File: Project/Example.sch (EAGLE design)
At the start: 13 parts, among them IC1 LM555D, J2 UX60-MB-5S8, Q1 BSS806N, Q2 SSM3J356R, SW1 MFS101D-6-Z

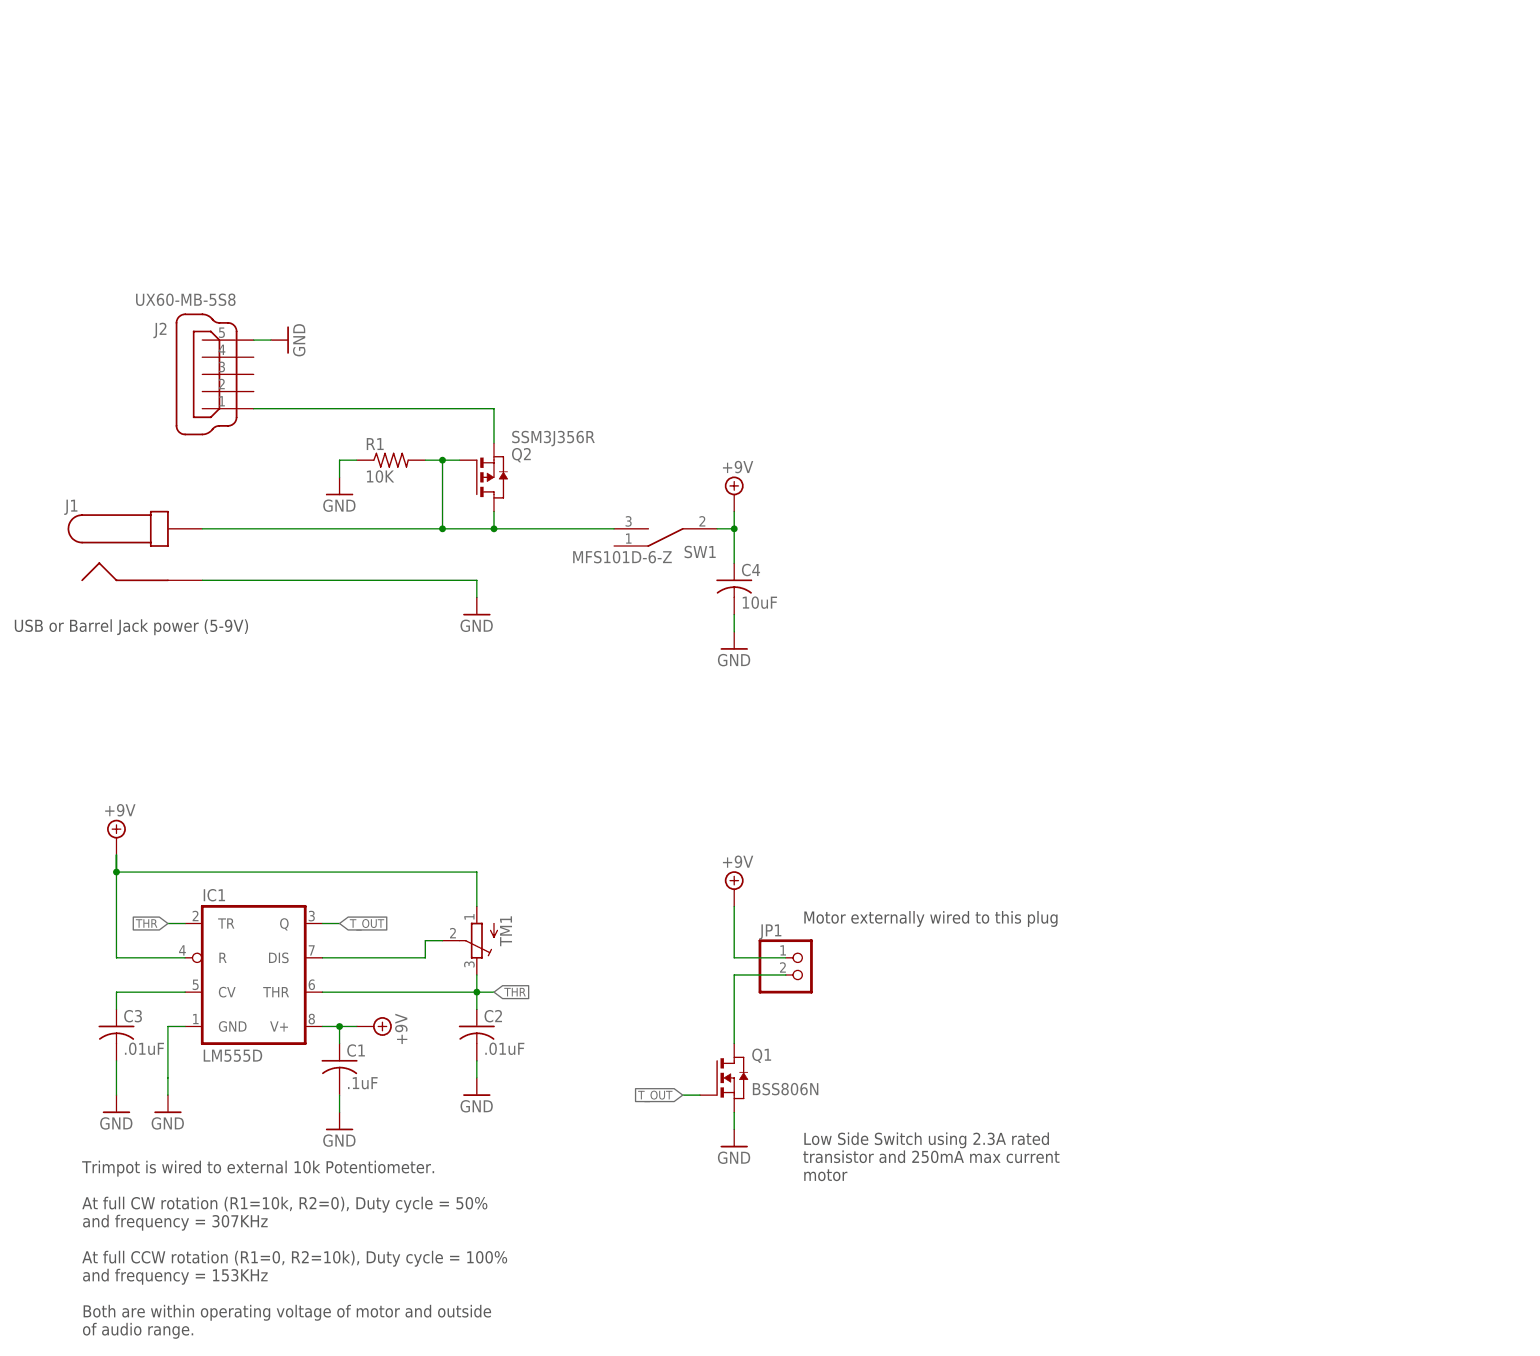
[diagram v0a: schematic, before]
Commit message: Made schematic neater
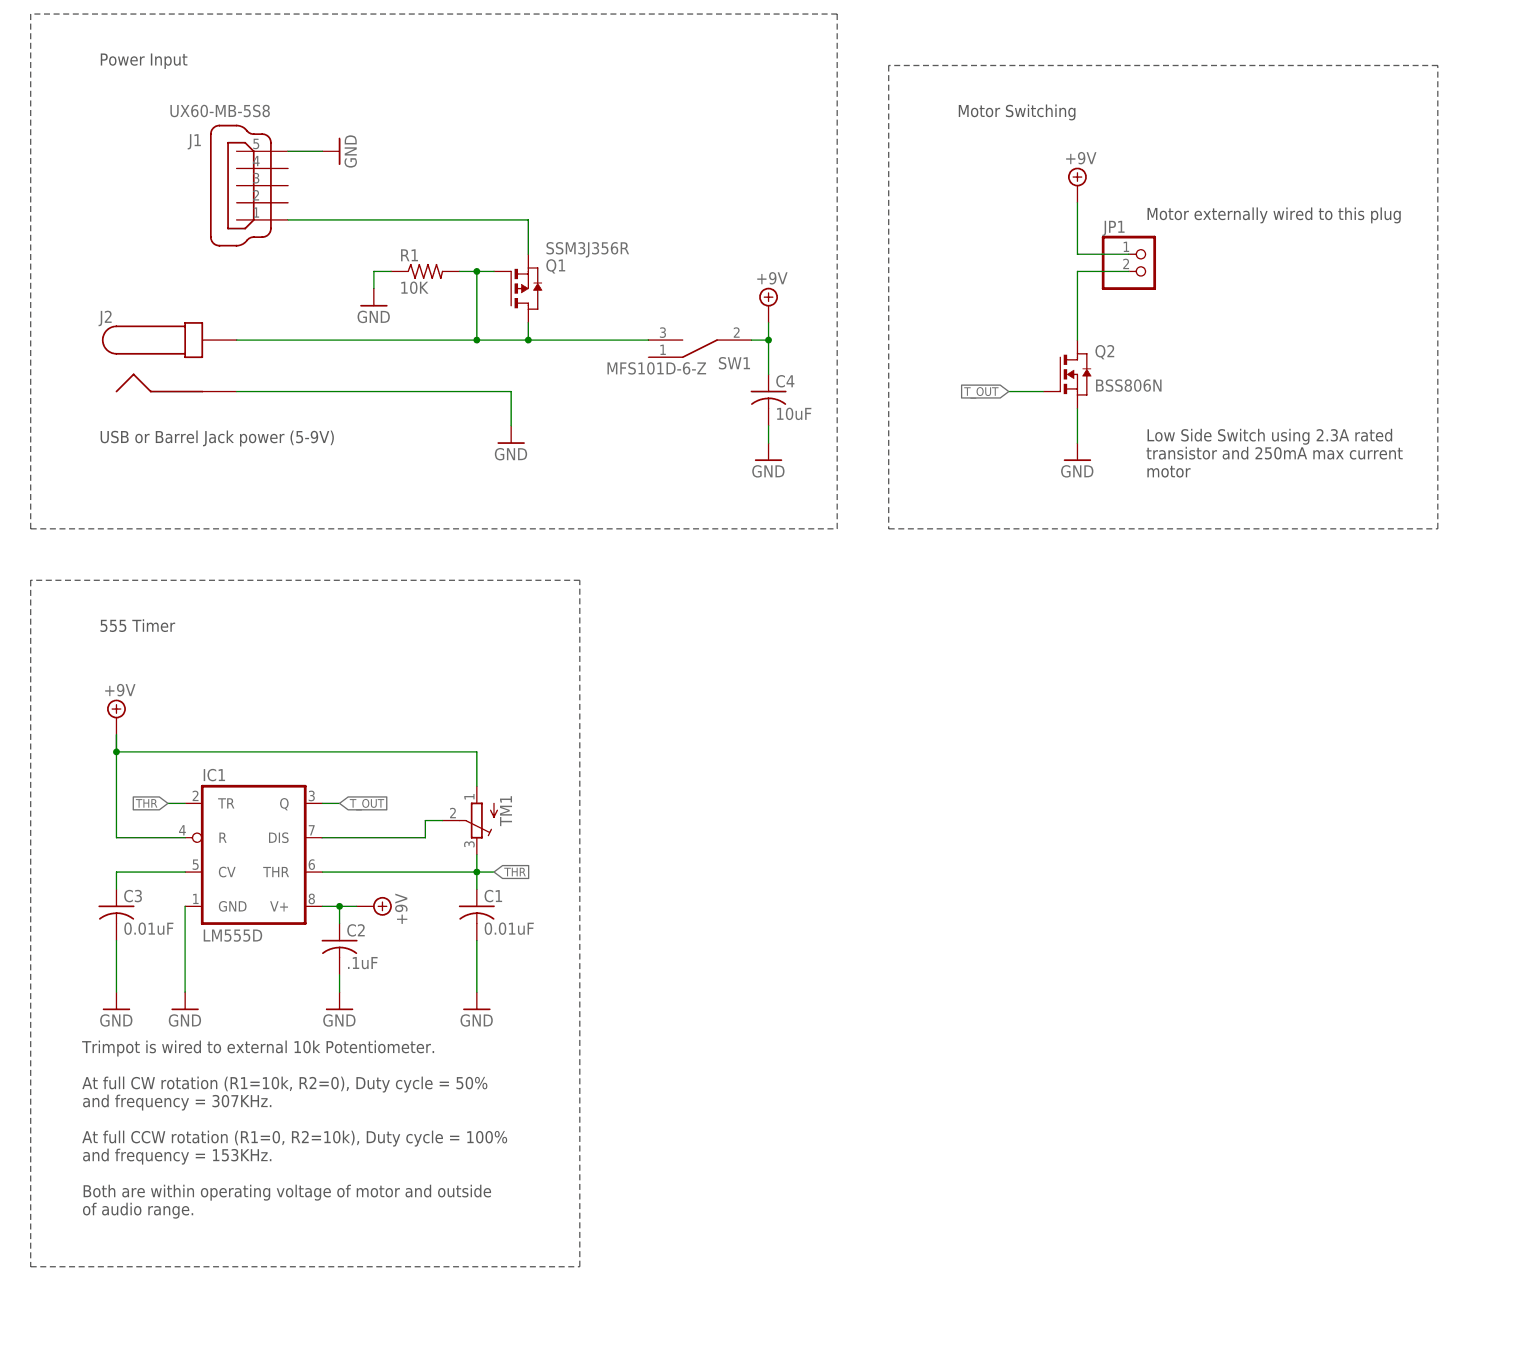
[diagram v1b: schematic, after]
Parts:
- C1: value .1uF -> 0.01uF
- C2: value .01uF -> .1uF
- C3: value .01uF -> 0.01uF
- J1: value (none) -> UX60-MB-5S8; device RoboJackets-Connectors:PJ-037A -> RoboJackets-Connectors:UX60-MB-5S8
- J2: value UX60-MB-5S8 -> (none); device RoboJackets-Connectors:UX60-MB-5S8 -> RoboJackets-Connectors:PJ-037A
- Q1: value BSS806N -> SSM3J356R; device RoboJackets-Discrete:BSS806N -> Example:SSM3J356R
- Q2: value SSM3J356R -> BSS806N; device Example:SSM3J356R -> RoboJackets-Discrete:BSS806N
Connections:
- net +9V: now also C2.1; no longer C1.1
- net GND: now also J1.5, J2.2, Q2.S; no longer J1.2, J2.5, Q1.S
- net N$2: now also Q2.D; no longer Q1.D
- net N$4: now also J1.1, Q1.S; no longer J2.1, Q2.S
- net N$6: now also J2.1, Q1.D, Q1.G; no longer J1.1, Q2.D, Q2.G
- net THR: now also C1.1; no longer C2.1
- net T_OUT: now also Q2.G; no longer Q1.G
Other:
- note added: "555 Timer"
- note added: "Motor Switching"
- note added: "Power Input"
- note added: "Trimpot is wired to external 10k Potentiometer. At full CW rotation (R1=10k, R2=0), Duty cycle = 50% and frequency = 307KHz. At full CCW rotation (R1=0, R2=10k), Duty cycle = 100% and frequency = 153KHz. Both are within operating voltage of motor and outside of audio range."
- note removed: "Trimpot is wired to external 10k Potentiometer. At full CW rotation (R1=10k, R2=0), Duty cycle = 50% and frequency = 307KHz At full CCW rotation (R1=0, R2=10k), Duty cycle = 100% and frequency = 153KHz Both are within operating voltage of motor and outside of audio range."
- moved on the sheet: C1, C2, C3, C4, IC1, JP1, Q1, Q2, R1, SW1, TM1

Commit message: Cleaning up example
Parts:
- C2: value .1uF -> 0.1uF
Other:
- note added: "Low side switch using 2.3A rated transistor and 450mA max current motor"
- note added: "Trimpot is wired to external 10K Potentiometer. At full CW rotation (R1=10K, R2=0), Duty cycle = 50% and frequency = 307KHz. At full CCW rotation (R1=0, R2=10K), Duty cycle = 100% and frequency = 153KHz. Both are within operating voltage of motor and outside of audio range."
- note removed: "Low Side Switch using 2.3A rated transistor and 250mA max current motor"
- note removed: "Trimpot is wired to external 10k Potentiometer. At full CW rotation (R1=10k, R2=0), Duty cycle = 50% and frequency = 307KHz. At full CCW rotation (R1=0, R2=10k), Duty cycle = 100% and frequency = 153KHz. Both are within operating voltage of motor and outside of audio range."
- moved on the sheet: JP1, Q2
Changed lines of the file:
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@@
 <part name="SUPPLY1" library="RoboJackets-Supplies" deviceset="+9V" device=""/>
 <part name="SUPPLY2" library="RoboJackets-Supplies" deviceset="+9V" device=""/>
-<part name="C2" library="rcl" library_urn="urn:adsk.eagle:library:334" deviceset="C-US" device="C0603" package3d_urn="urn:adsk.eagle:package:23616/2" value=".1uF"/>
+<part name="C2" library="rcl" library_urn="urn:adsk.eagle:library:334" deviceset="C-US" device="C0603" package3d_urn="urn:adsk.eagle:package:23616/2" value="0.1uF"/>
 <part name="C1" library="rcl" library_urn="urn:adsk.eagle:library:334" deviceset="C-US" device="C0603" package3d_urn="urn:adsk.eagle:package:23616/2" value="0.01uF"/>
 <part name="SUPPLY3" library="RoboJackets-Supplies" deviceset="GND" device=""/>
@@
 <description>555 Timer Motor Driver Circuit</description>
 <plain>
-<text x="22.86" y="25.4" size="1.778" layer="97">Trimpot is wired to external 10k Potentiometer.
-At full CW rotation (R1=10k, R2=0), Duty cycle = 50%
+<text x="25.4" y="25.4" size="1.778" layer="97">Trimpot is wired to external 10K Potentiometer.
+At full CW rotation (R1=10K, R2=0), Duty cycle = 50%
 and frequency = 307KHz.
-At full CCW rotation (R1=0, R2=10k), Duty cycle = 100%
+At full CCW rotation (R1=0, R2=10K), Duty cycle = 100%
 and frequency = 153KHz.
 Both are within operating voltage of motor and outside
 of audio range. </text>
-<text x="180.34" y="172.72" size="1.778" layer="97">Motor externally wired to this plug</text>
-<text x="180.34" y="134.62" size="1.778" layer="97">Low Side Switch using 2.3A rated
-transistor and 250mA max current
+<text x="182.88" y="172.72" size="1.778" layer="97">Motor externally wired to this plug</text>
+<text x="182.88" y="134.62" size="1.778" layer="97">Low side switch using 2.3A rated
+transistor and 450mA max current
 motor</text>
 <text x="25.4" y="139.7" size="1.778" layer="97">USB or Barrel Jack power (5-9V)</text>
-<wire x1="15.24" y1="127" x2="134.62" y2="127" width="0.1524" layer="97" style="shortdash"/>
-<wire x1="134.62" y1="127" x2="134.62" y2="203.2" width="0.1524" layer="97" style="shortdash"/>
-<wire x1="134.62" y1="203.2" x2="15.24" y2="203.2" width="0.1524" layer="97" style="shortdash"/>
+<wire x1="15.24" y1="127" x2="137.16" y2="127" width="0.1524" layer="97" style="shortdash"/>
+<wire x1="137.16" y1="127" x2="137.16" y2="203.2" width="0.1524" layer="97" style="shortdash"/>
+<wire x1="137.16" y1="203.2" x2="15.24" y2="203.2" width="0.1524" layer="97" style="shortdash"/>
 <wire x1="15.24" y1="203.2" x2="15.24" y2="127" width="0.1524" layer="97" style="shortdash"/>
 <text x="25.4" y="195.58" size="1.778" layer="97">Power Input</text>
 <wire x1="15.24" y1="119.38" x2="15.24" y2="17.78" width="0.1524" layer="97" style="shortdash"/>
-<wire x1="15.24" y1="17.78" x2="96.52" y2="17.78" width="0.1524" layer="97" style="shortdash"/>
-<wire x1="96.52" y1="17.78" x2="96.52" y2="119.38" width="0.1524" layer="97" style="shortdash"/>
-<wire x1="96.52" y1="119.38" x2="15.24" y2="119.38" width="0.1524" layer="97" style="shortdash"/>
+<wire x1="15.24" y1="17.78" x2="99.06" y2="17.78" width="0.1524" layer="97" style="shortdash"/>
+<wire x1="99.06" y1="17.78" x2="99.06" y2="119.38" width="0.1524" layer="97" style="shortdash"/>
+<wire x1="99.06" y1="119.38" x2="15.24" y2="119.38" width="0.1524" layer="97" style="shortdash"/>
 <text x="25.4" y="111.76" size="1.778" layer="97">555 Timer</text>
-<wire x1="142.24" y1="127" x2="223.52" y2="127" width="0.1524" layer="97" style="shortdash"/>
-<wire x1="223.52" y1="127" x2="223.52" y2="195.58" width="0.1524" layer="97" style="shortdash"/>
-<wire x1="223.52" y1="195.58" x2="142.24" y2="195.58" width="0.1524" layer="97" style="shortdash"/>
-<wire x1="142.24" y1="195.58" x2="142.24" y2="127" width="0.1524" layer="97" style="shortdash"/>
-<text x="152.4" y="187.96" size="1.778" layer="97">Motor Switching</text>
+<wire x1="144.78" y1="127" x2="228.6" y2="127" width="0.1524" layer="97" style="shortdash"/>
+<wire x1="228.6" y1="127" x2="228.6" y2="195.58" width="0.1524" layer="97" style="shortdash"/>
+<wire x1="228.6" y1="195.58" x2="144.78" y2="195.58" width="0.1524" layer="97" style="shortdash"/>
+<wire x1="144.78" y1="195.58" x2="144.78" y2="127" width="0.1524" layer="97" style="shortdash"/>
+<text x="154.94" y="187.96" size="1.778" layer="97">Motor Switching</text>
 </plain>
 <instances>
@@
 <attribute name="VALUE" x="28.956" y="66.929" size="1.778" layer="96"/>
 </instance>
-<instance part="Q2" gate="G$1" x="170.18" y="149.86" smashed="yes">
-<attribute name="VALUE" x="172.72" y="147.32" size="1.778" layer="96"/>
-<attribute name="NAME" x="172.72" y="152.4" size="1.778" layer="95"/>
-</instance>
-<instance part="SUPPLY6" gate="G$1" x="170.18" y="137.16" smashed="yes">
-<attribute name="VALUE" x="167.64" y="134.62" size="1.778" layer="96"/>
+<instance part="Q2" gate="G$1" x="172.72" y="149.86" smashed="yes">
+<attribute name="VALUE" x="175.26" y="147.32" size="1.778" layer="96"/>
+<attribute name="NAME" x="175.26" y="152.4" size="1.778" layer="95"/>
+</instance>
+<instance part="SUPPLY6" gate="G$1" x="172.72" y="137.16" smashed="yes">
+<attribute name="VALUE" x="170.18" y="134.62" size="1.778" layer="96"/>
 </instance>
 <instance part="J2" gate="G$1" x="35.56" y="149.86" smashed="yes">
@@
 <attribute name="VALUE" x="25.4" y="144.78" size="1.778" layer="96"/>
 </instance>
-<instance part="JP1" gate="G$1" x="180.34" y="165.1" smashed="yes">
-<attribute name="NAME" x="173.99" y="170.815" size="1.778" layer="95"/>
-<attribute name="VALUE" x="173.99" y="160.02" size="1.778" layer="96"/>
-</instance>
-<instance part="SUPPLY7" gate="+9V" x="170.18" y="177.8" smashed="yes">
-<attribute name="VALUE" x="168.275" y="180.975" size="1.778" layer="96"/>
-</instance>
-<instance part="SUPPLY8" gate="G$1" x="86.36" y="139.7" smashed="yes">
-<attribute name="VALUE" x="83.82" y="137.16" size="1.778" layer="96"/>
+<instance part="JP1" gate="G$1" x="182.88" y="165.1" smashed="yes">
+<attribute name="NAME" x="176.53" y="170.815" size="1.778" layer="95"/>
+<attribute name="VALUE" x="176.53" y="160.02" size="1.778" layer="96"/>
+</instance>
+<instance part="SUPPLY7" gate="+9V" x="172.72" y="177.8" smashed="yes">
+<attribute name="VALUE" x="170.815" y="180.975" size="1.778" layer="96"/>
+</instance>
+<instance part="SUPPLY8" gate="G$1" x="86.36" y="137.16" smashed="yes">
+<attribute name="VALUE" x="83.82" y="134.62" size="1.778" layer="96"/>
 </instance>
 <instance part="SUPPLY9" gate="+9V" x="124.46" y="160.02" smashed="yes">
@@
 <pinref part="SUPPLY6" gate="G$1" pin="GND"/>
 <pinref part="Q2" gate="G$1" pin="S"/>
-<wire x1="170.18" y1="139.7" x2="170.18" y2="144.78" width="0.1524" layer="91"/>
+<wire x1="172.72" y1="139.7" x2="172.72" y2="144.78" width="0.1524" layer="91"/>
 </segment>
 <segment>
@@
 <wire x1="45.72" y1="147.32" x2="86.36" y2="147.32" width="0.1524" layer="91"/>
 <pinref part="SUPPLY8" gate="G$1" pin="GND"/>
-<wire x1="86.36" y1="147.32" x2="86.36" y2="142.24" width="0.1524" layer="91"/>
+<wire x1="86.36" y1="147.32" x2="86.36" y2="139.7" width="0.1524" layer="91"/>
 </segment>
 <segment>
@@
 <segment>
 <pinref part="JP1" gate="G$1" pin="1"/>
-<wire x1="177.8" y1="167.64" x2="170.18" y2="167.64" width="0.1524" layer="91"/>
-<wire x1="170.18" y1="167.64" x2="170.18" y2="175.26" width="0.1524" layer="91"/>
+<wire x1="180.34" y1="167.64" x2="172.72" y2="167.64" width="0.1524" layer="91"/>
+<wire x1="172.72" y1="167.64" x2="172.72" y2="175.26" width="0.1524" layer="91"/>
 <pinref part="SUPPLY7" gate="+9V" pin="+9V"/>
 </segment>
@@
 <segment>
 <pinref part="Q2" gate="G$1" pin="G"/>
-<wire x1="165.1" y1="147.32" x2="160.02" y2="147.32" width="0.1524" layer="91"/>
-<label x="160.02" y="147.32" size="1.27" layer="95" rot="R180" xref="yes"/>
+<wire x1="167.64" y1="147.32" x2="162.56" y2="147.32" width="0.1524" layer="91"/>
+<label x="162.56" y="147.32" size="1.27" layer="95" rot="R180" xref="yes"/>
 </segment>
 </net>
@@
 <pinref part="JP1" gate="G$1" pin="2"/>
 <pinref part="Q2" gate="G$1" pin="D"/>
-<wire x1="177.8" y1="165.1" x2="170.18" y2="165.1" width="0.1524" layer="91"/>
-<wire x1="170.18" y1="165.1" x2="170.18" y2="154.94" width="0.1524" layer="91"/>
-</segment>
-</net>
+<wire x1="180.34" y1="165.1" x2="172.72" y2="165.1" width="0.1524" layer="91"/>
+<wire x1="172.72" y1="165.1" x2="172.72" y2="154.94" width="0.1524" layer="91"/>
+</segment>
+</net>

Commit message: Wrote a thing
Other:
- note added: "Motor"
- note removed: "Motor Switching"
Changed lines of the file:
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@@
 <wire x1="228.6" y1="195.58" x2="144.78" y2="195.58" width="0.1524" layer="97" style="shortdash"/>
 <wire x1="144.78" y1="195.58" x2="144.78" y2="127" width="0.1524" layer="97" style="shortdash"/>
-<text x="154.94" y="187.96" size="1.778" layer="97">Motor Switching</text>
+<text x="154.94" y="187.96" size="1.778" layer="97">Motor</text>
 </plain>
 <instances>
